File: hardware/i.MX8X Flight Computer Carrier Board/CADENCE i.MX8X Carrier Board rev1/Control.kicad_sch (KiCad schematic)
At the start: 0 parts

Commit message: Sheet Organization
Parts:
- added SW1: SW_DIP_x04, symbol Switch:SW_DIP_x04
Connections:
- new net +3.3V: SW1.5, SW1.6, SW1.7, SW1.8
- new net X_BOOT_MODE0: SW1.1
- new net X_BOOT_MODE1: SW1.2
- new net X_BOOT_MODE2: SW1.3
- new net X_BOOT_MODE3: SW1.4
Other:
- note added: "Boot Mode Control"

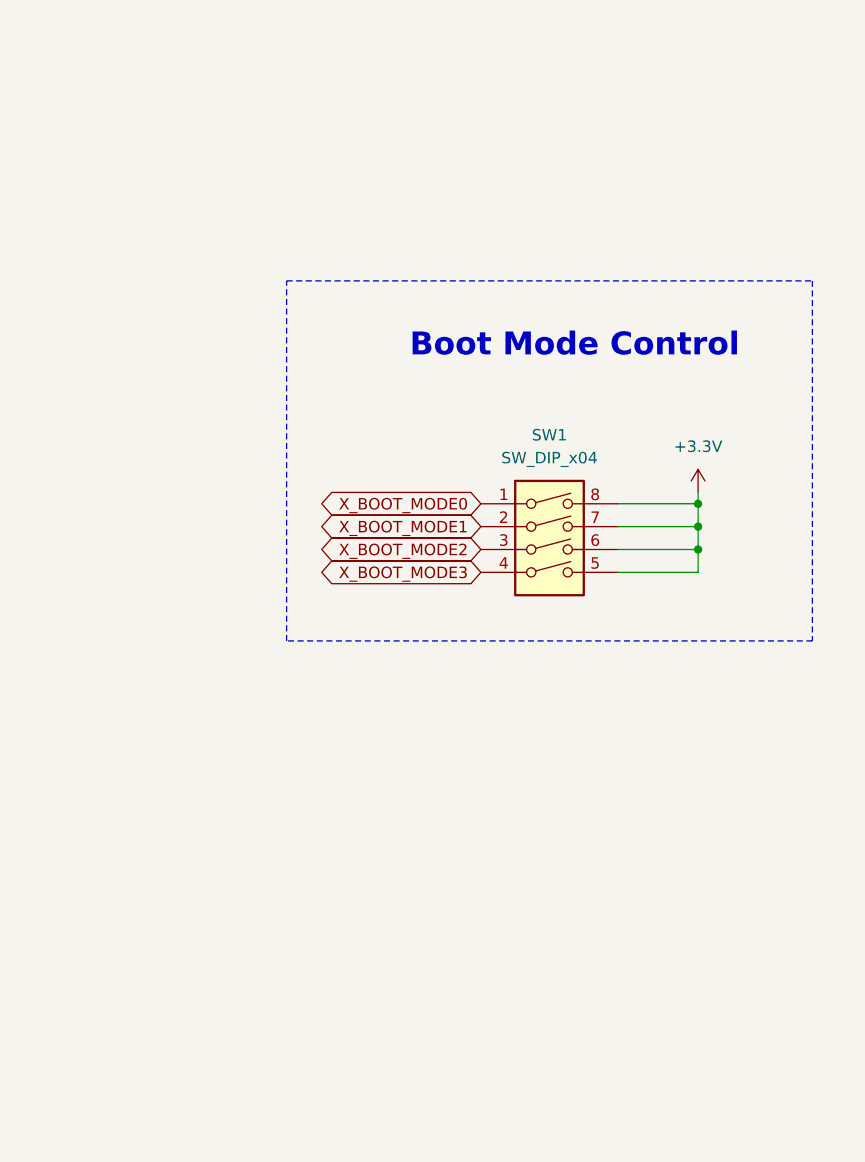
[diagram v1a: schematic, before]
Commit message: updated connections
-reset button
- fixed boot mode select
- i2c reorg/fixes
-added satnogs power monitor
-heater trigger connection (2gpio)
-more additions/fixes
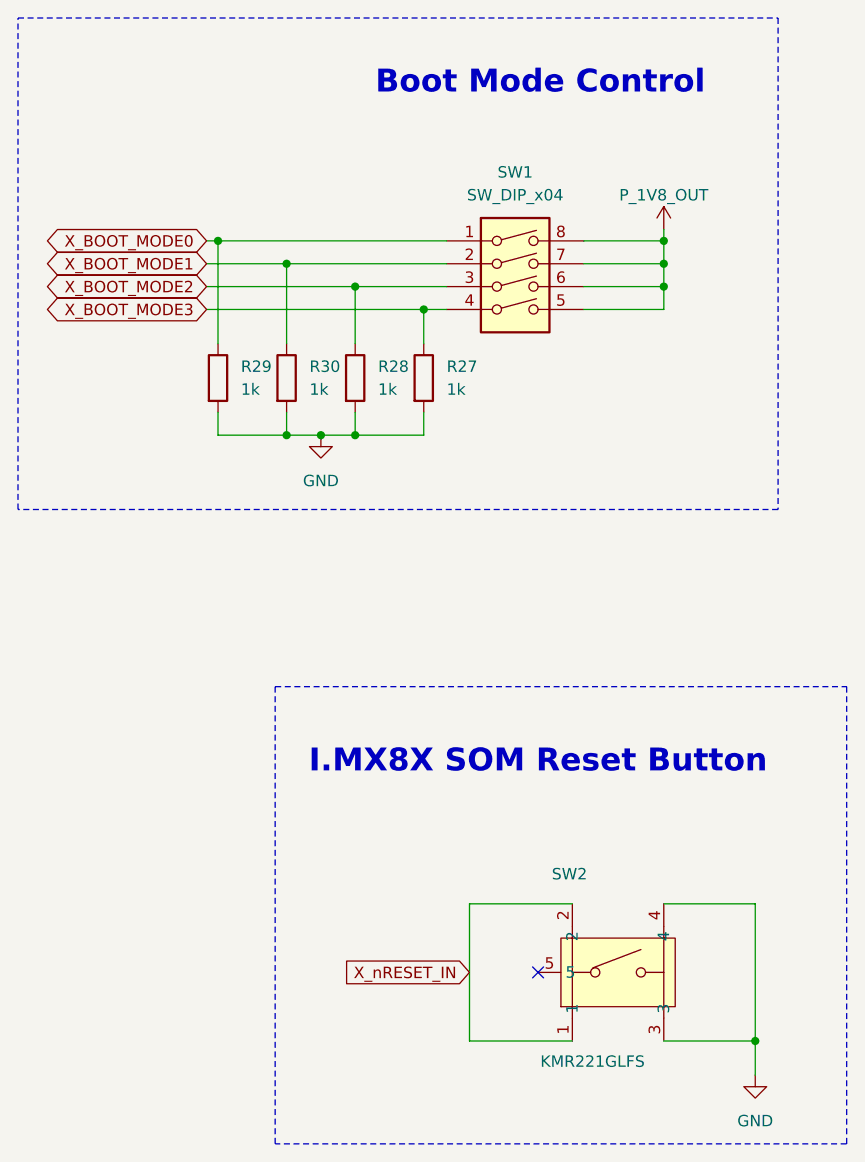
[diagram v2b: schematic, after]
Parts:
- added R27, R28, R29, R30: 1k, symbol Device:R
- added SW2: KMR221GLFS, imx8_carrier_board_footprints:KEY-SMD_KMR2XXGXXX, symbol imx8_carrier_board_symbol_library:KMR221GLFS
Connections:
- net X_BOOT_MODE0: now also R29.1
- net X_BOOT_MODE1: now also R30.1
- net X_BOOT_MODE2: now also R28.1
- net X_BOOT_MODE3: now also R27.1
- net +3.3V renamed P_1V8_OUT
- new net GND: R27.2, R28.2, R29.2, R30.2, SW2.3, SW2.4
- new net X_nRESET_IN: SW2.1, SW2.2
- no-connect marks 0 -> 1
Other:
- note added: "I.MX8X SOM Reset Button"
- moved on the sheet: SW1

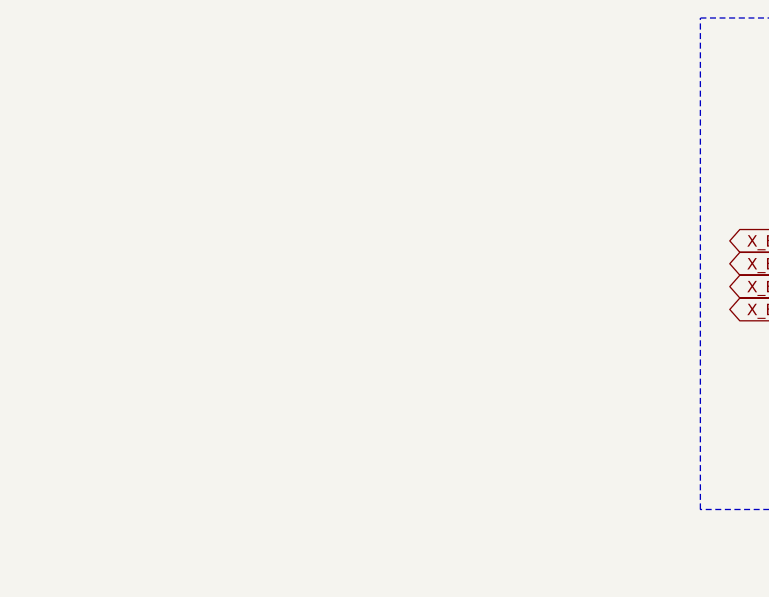
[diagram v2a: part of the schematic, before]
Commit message: power system updates and more
- replaced old cots regulators with SEE tested LT8612 buck regulators and LM1085 3.3V fixed version (up to 3A, tested to 6krad), have not deleted old regulators yet tho
- rearranged spi and i2c connections to allow for additional 3.3v i2c bus
- added power header pins (maybe add 1 more gnd header)
- added application notes around various components
- removed i2c bus from satnogs and implemented power monitor for satnogs
- added overall power switch
-fixed issue with i2c buffer connections
-performed preliminary onboard power current/power use with variety of cases
-to do: add LEDs
- to do: look for more mosfet/load switch to implement power cycling
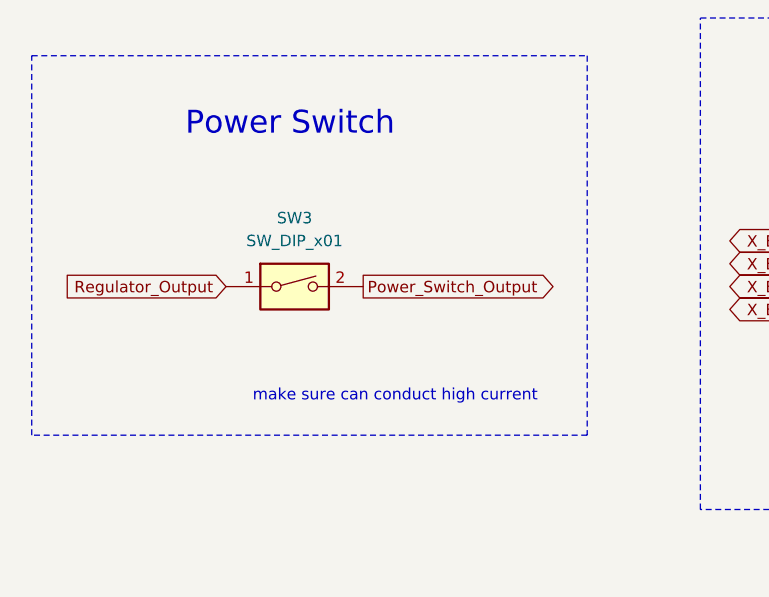
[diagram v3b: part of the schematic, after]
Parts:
- added SW3: SW_DIP_x01, symbol Switch:SW_DIP_x01
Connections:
- new net Power_Switch_Output: SW3.2
- new net Regulator_Output: SW3.1
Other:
- note added: "Power Switch"
- note added: "make sure can conduct high current"
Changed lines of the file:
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@@
+		)
+	)
+	(rectangle
+		(start 81.28 41.656)
+		(end 143.002 83.82)
+		(stroke
+			(width 0)
+			(type dash)
+		)
+		(fill
+			(type none)
+		)
+	)
+	(text "Power Switch"
+		(exclude_from_sim no)
+		(at 109.982 49.276 0)
+		(effects
+			(font
+				(size 2.54 2.54)
+				(thickness 0.3175)
+			)
+		)
+	)
+	(text "make sure can conduct high current"
+		(exclude_from_sim no)
+		(at 121.666 79.502 0)
+		(effects
+			(font
+				(size 1.27 1.27)
+			)
 		)
 	)
@@
 		)
 	)
+	(global_label "Regulator_Output"
+		(shape input)
+		(at 102.87 67.31 180)
+		(fields_autoplaced yes)
+		(effects
+			(font
+				(size 1.27 1.27)
+			)
+			(justify right)
+		)
+		(property "Intersheetrefs" "${INTERSHEET_REFS}"
+			(at 83.5566 67.31 0)
+			(effects
+				(font
+					(size 1.27 1.27)
+				)
+				(justify right)
+				(hide yes)
+			)
+		)
+	)
 	(global_label "X_BOOT_MODE1"
 		(shape bidirectional)
@@
 					(size 1.27 1.27)
 				)
+				(hide yes)
+			)
+		)
+	)
+	(global_label "Power_Switch_Output"
+		(shape output)
+		(at 118.11 67.31 0)
+		(fields_autoplaced yes)
+		(effects
+			(font
+				(size 1.27 1.27)
+			)
+			(justify left)
+		)
+		(property "Intersheetrefs" "${INTERSHEET_REFS}"
+			(at 140.9917 67.31 0)
+			(effects
+				(font
+					(size 1.27 1.27)
+				)
+				(justify left)
 				(hide yes)
 			)
@@
 					(unit 1)
 				)
+			)
+		)
+	)
+	(symbol
+		(lib_id "Switch:SW_DIP_x01")
+		(at 110.49 67.31 0)
+		(unit 1)
+		(exclude_from_sim no)
+		(in_bom yes)
+		(on_board yes)
+		(dnp no)
+		(fields_autoplaced yes)
+		(property "Reference" "SW3"
+			(at 110.49 59.69 0)
+			(effects
+				(font
+					(size 1.27 1.27)
+				)
+			)
+		)
+		(property "Value" "SW_DIP_x01"
+			(at 110.49 62.23 0)
+			(effects
+				(font
+					(size 1.27 1.27)
+				)
+			)
+		)
+		(property "Footprint" ""
+			(at 110.49 67.31 0)
+			(effects
+				(font
+					(size 1.27 1.27)
+				)
+				(hide yes)
+			)
+		)
+		(property "Datasheet" "~"
+			(at 110.49 67.31 0)
+			(effects
+				(font
+					(size 1.27 1.27)
+				)
+				(hide yes)
+			)
+		)
+		(property "Description" "1x DIP Switch, Single Pole Single Throw (SPST) switch, small symbol"
+			(at 110.49 67.31 0)
+			(effects
+				(font
+					(size 1.27 1.27)
+				)
+				(hide yes)
+			)
+		)
+		(pin "1"
+		)
+		(pin "2"
+		)
+		(instances
+			(project ""
+				(path "/de284495-d382-47cb-b528-76e440980d40/089c604b-0863-4822-93dd-cc06ae04e525"
+					(reference "SW3")
+					(unit 1)
+				)

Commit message: meeting changes
-watchdog
-notes
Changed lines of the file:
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@@
+	(wire
+		(pts
+			(xy 189.23 85.09) (xy 189.23 83.82)
+		)
+		(stroke
+			(width 0)
+			(type default)
+		)
+	)
 	(wire
 		(pts
@@
 	(symbol
 		(lib_id "power:GND")
-		(at 189.23 83.82 0)
+		(at 189.23 85.09 0)
 		(unit 1)
 		(exclude_from_sim no)
@@
 		(fields_autoplaced yes)
 		(property "Reference" "#PWR016"
+			(at 189.23 91.44 0)
+			(effects
+				(font
+					(size 1.27 1.27)
+				)
+				(hide yes)
+			)
+		)
+		(property "Value" "GND"
 			(at 189.23 90.17 0)
 			(effects
@@
 					(size 1.27 1.27)
 				)
-				(hide yes)
-			)
-		)
-		(property "Value" "GND"
-			(at 189.23 88.9 0)
-			(effects
-				(font
-					(size 1.27 1.27)
-				)
 			)
 		)
 		(property "Footprint" ""
-			(at 189.23 83.82 0)
+			(at 189.23 85.09 0)
 			(effects
 				(font
@@
 		)
 		(property "Datasheet" ""
-			(at 189.23 83.82 0)
+			(at 189.23 85.09 0)
 			(effects
 				(font
@@
 		)
 		(property "Description" "Power symbol creates a global label with name \"GND\" , ground"
-			(at 189.23 83.82 0)
-			(effects
-				(font
+			(at 189.23 85.09 0)
+			(effects
+				(font

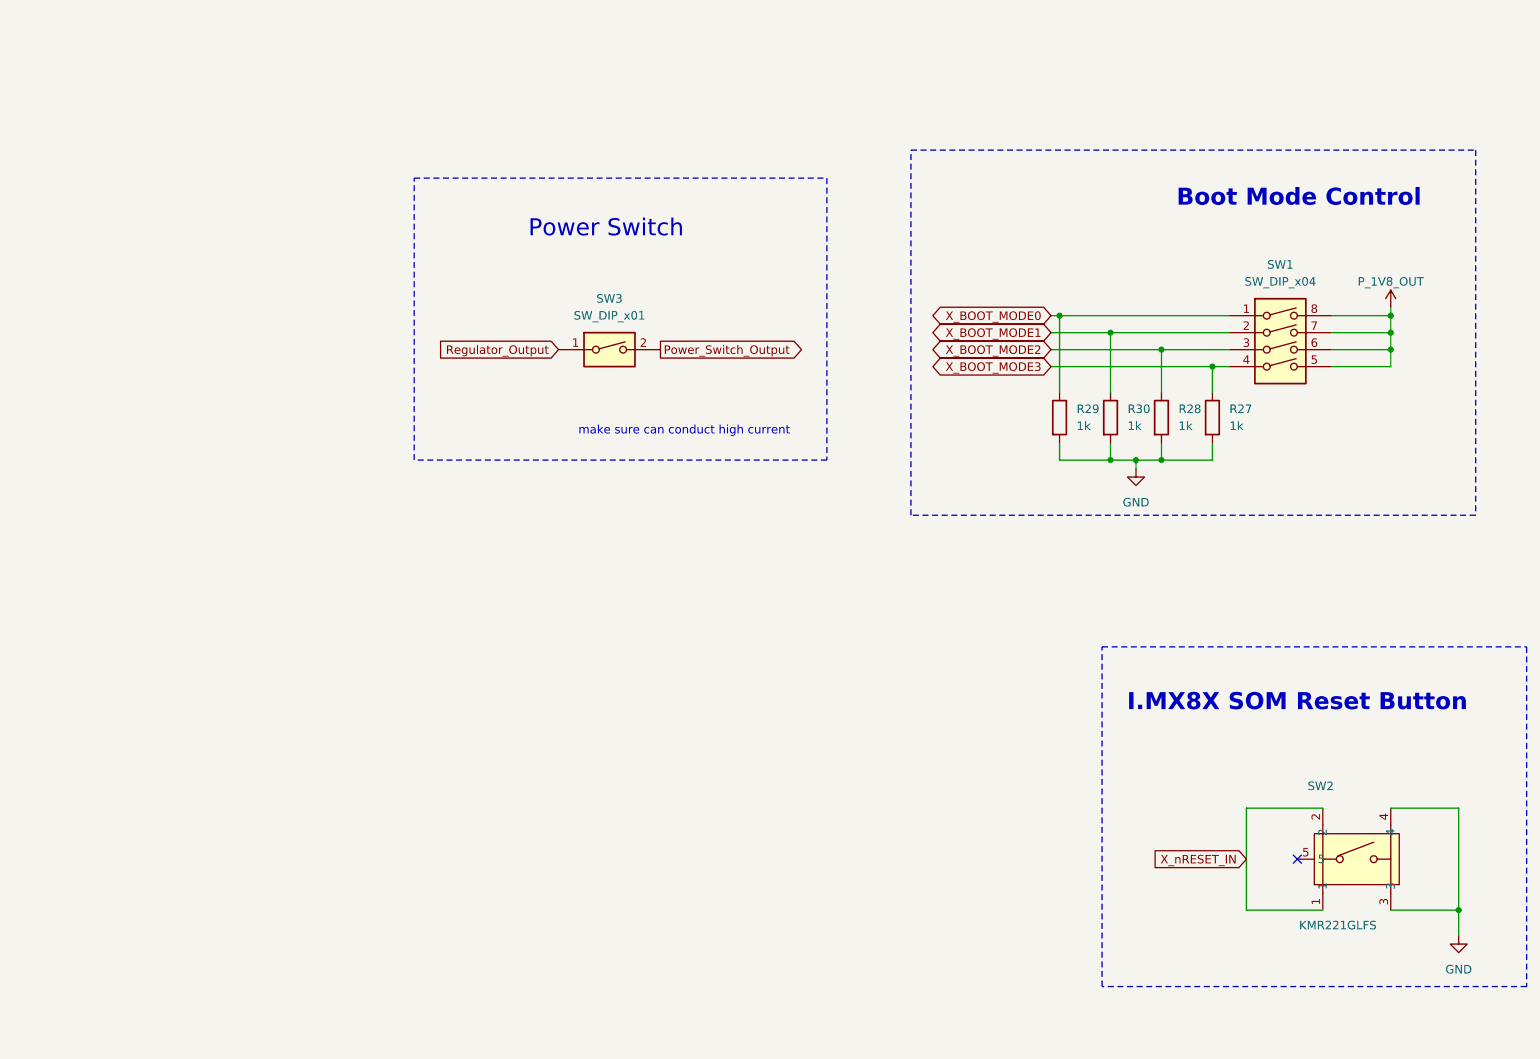
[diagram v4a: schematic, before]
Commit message: added some LEDs, fixed few power nets
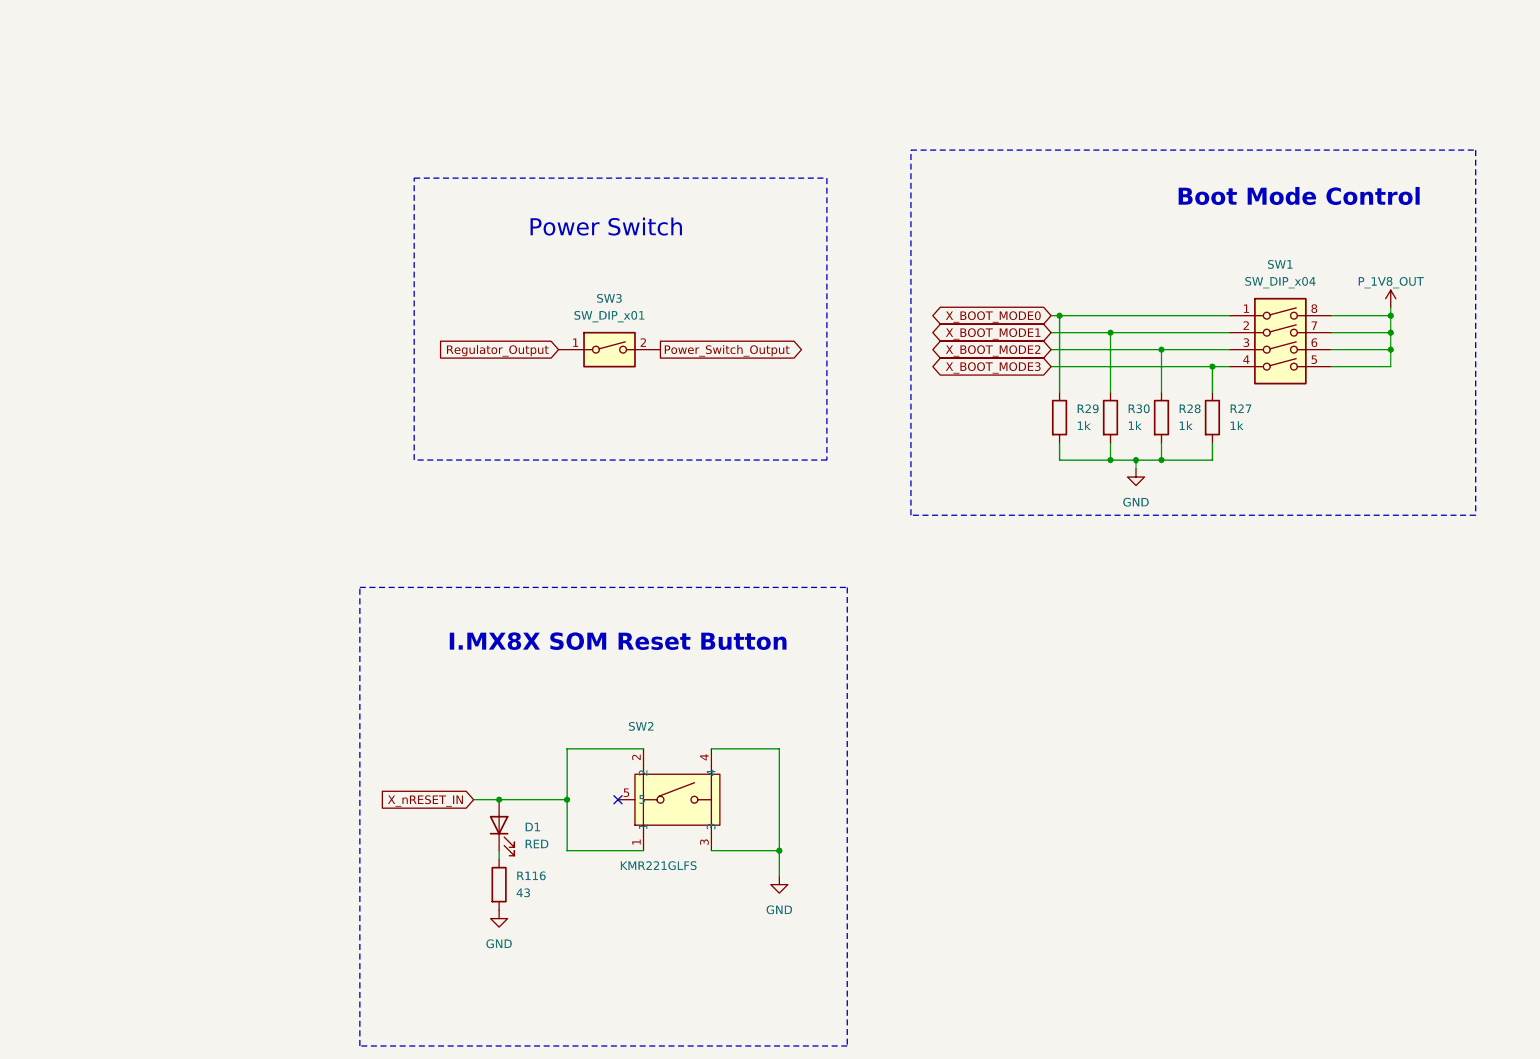
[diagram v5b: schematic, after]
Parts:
- added D1: RED, symbol Device:LED
- added R116: 43, symbol Device:R
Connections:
- net GND: now also R116.2
- net X_nRESET_IN: now also D1.2 (A)
- new net: D1.1 (K), R116.1
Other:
- note removed: "make sure can conduct high current"
- moved on the sheet: SW2

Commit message: schematic reorg
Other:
- moved on the sheet: D1, R116, R27, R28, R29, R30, SW1, SW2, SW3
